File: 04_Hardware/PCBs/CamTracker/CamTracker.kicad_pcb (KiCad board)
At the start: 6 copper layers, 126.2 x 49.2 mm, 403 parts, among them IC1 W25Q128JVSIM, IC2 AP7361E-33FGE-7, IC3 AP7361E-33FGE-7, J1 PJ-059A, J10 1.25x15P, J11 22-28-4034, J12 22-28-4034, J13 SIM8066-6-1-14-01-A, J14 MEM2061-01-188-00-A, J15 636101112001, J16 636101112001, J17 636101112001, J18 636101112001, J2 67996-100HLF, J21 67996-100HLF, J22 USB3076-30-A, J27 53047-0210, J28 Bus_M.2_Socket_M, J3 67996-100HLF, J5 22-28-4034, J6 USB4080-03-A, J7 22-28-4044, J9 1.25x15P, Q1 BC817-40,215, Q10 BC817-40,215, Q11 BC817-40,215, Q2 BC817-40,215, Q3 BC817-40,215, Q4 BC817-40,215, Q5 BC817-40,215, Q6 BC817-40,215, Q9 BC817-40,215, U1 SC206EEMDA-G51-UGNDA, U10 SGM804, U11 ST4SI2M0020TPIFW, U12 RP2040, U13 PAM8302AASCR, U14 ASM2362, U15 AP61100Z6-7, U2 AP64502QSP-13, U3 AP7335-WG-7, U4 AP22654QWU-7, U6 AP61300Z6-7, U7 PI3USB4000DZUAEX, U9 PI3USB4000DZUAEX, Y1 ABM8-272-T3, Y2 25MHz

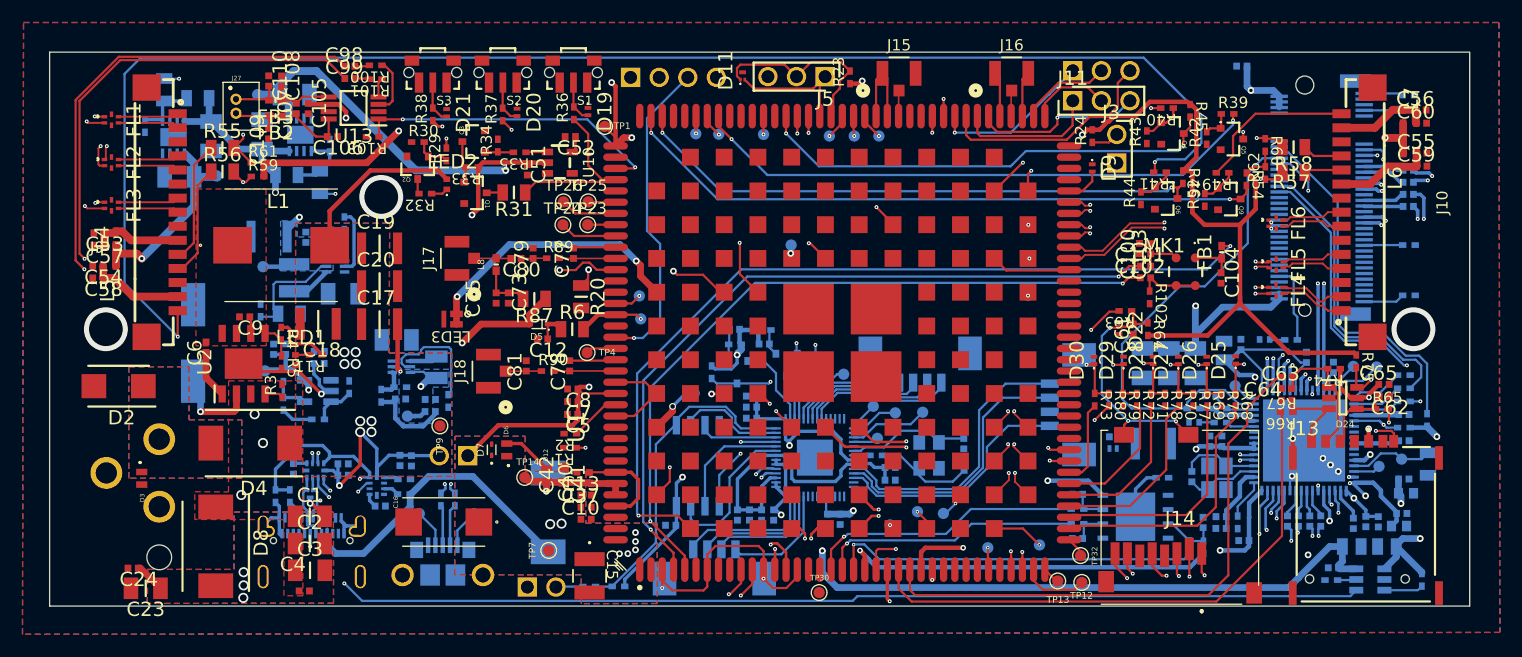
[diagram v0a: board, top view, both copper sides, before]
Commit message: feat(layout): Completed routing of all traces but with Errors DRCs
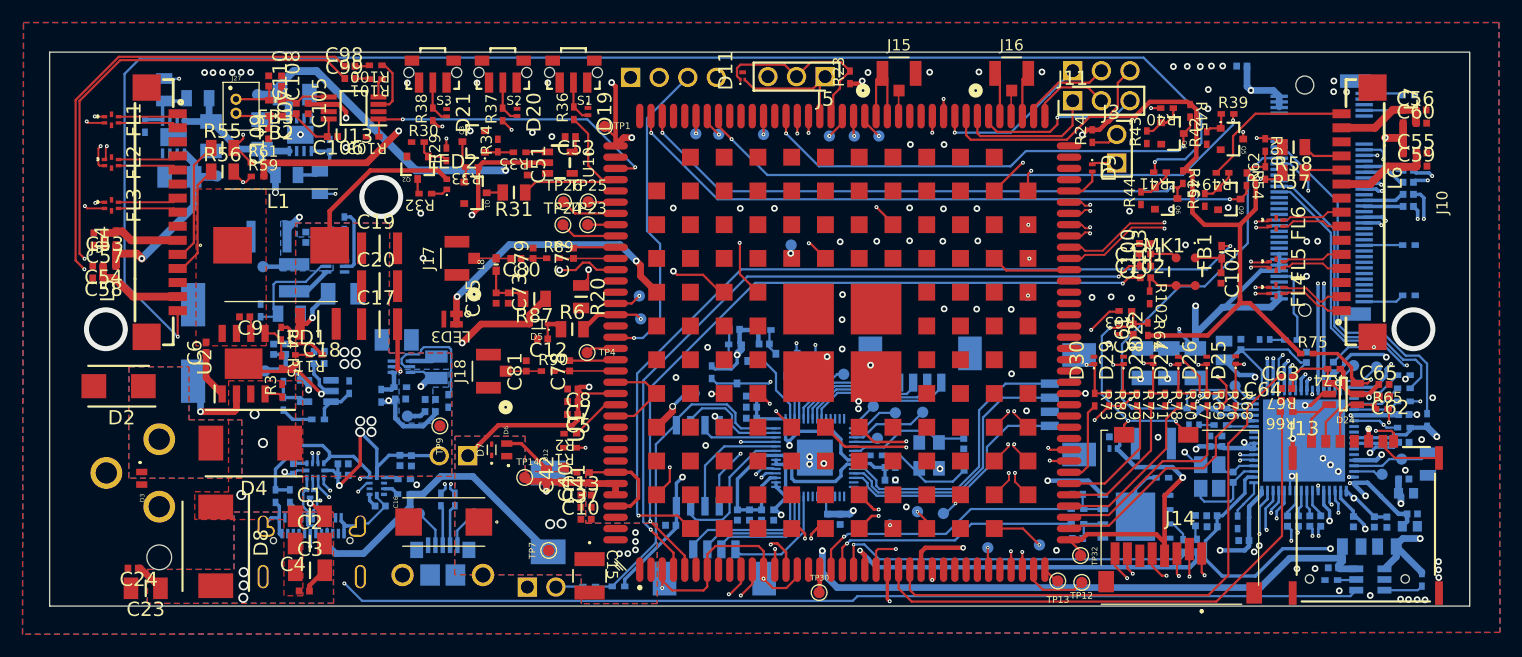
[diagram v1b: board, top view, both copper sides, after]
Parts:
- moved R75 4.43 mm to (181.5, 85.8), turned to 0 degrees
- moved C148 3.67 mm to (174.9, 96.8)
- moved C138 0.96 mm to (190.6, 101.2)
- moved C140 0.94 mm to (190.8, 100.1)
- moved C147 0.82 mm to (173.0, 100.2)
- moved C142 0.79 mm to (173.1, 101.2)
- moved C129 0.76 mm to (187.5, 100.8)
- moved C133 0.76 mm to (188.6, 100.8)
- moved TP39 0.75 mm to (188.1, 96.5)
- moved C70 0.70 mm to (171.6, 100.7)
- moved Y2 0.65 mm to (172.8, 96.7)
- moved R83 0.59 mm to (170.5, 102.9)
- moved R84 0.59 mm to (171.7, 102.9)
- moved D24 0.36 mm to (184.7, 89.4)
- moved LED5 0.22 mm to (171.4, 92.1)
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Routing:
- net NVMe_1V05: track 179.3 -> 225.9 mm, vias 7 -> 11
- net GND: track 134.3 -> 174.2 mm, vias 15 -> 121
- net NVMe_3V3: track 253.4 -> 292.1 mm, vias 6 -> 10
- net /SIM_SD/SD_VDD: track 1.82 -> 29.3 mm, vias 0 -> 1
- net SD_LDO4: track 36.4 -> 60.2 mm, vias 2 -> 6
- net NVMe_2V5: track 37.9 -> 61.1 mm, vias 5 -> 6
- net LDO15A_1V8: track 206.7 -> 201.7 mm
- net /SIM_SD/USIM1_DET: track 73.7 -> 78.6 mm
- net Net-(U14-XO): track 7.08 -> 3.65 mm
- net Net-(U1F-SD_CLK): track 23.5 -> 20.9 mm
- net Net-(U1E-USB_BOOT): track 29.8 -> 32.0 mm
- net Net-(U1F-USIM2_DET): track 0.00 -> 2.06 mm
- net Net-(U1F-SD_CMD): track 21.0 -> 18.9 mm
- net /SIM_SD/USIM1_VDD: track 69.1 -> 70.2 mm
- net /Audio/MIC1_P: track 66.3 -> 67.4 mm
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
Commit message: feat(layout): Resolved all DRC Errors
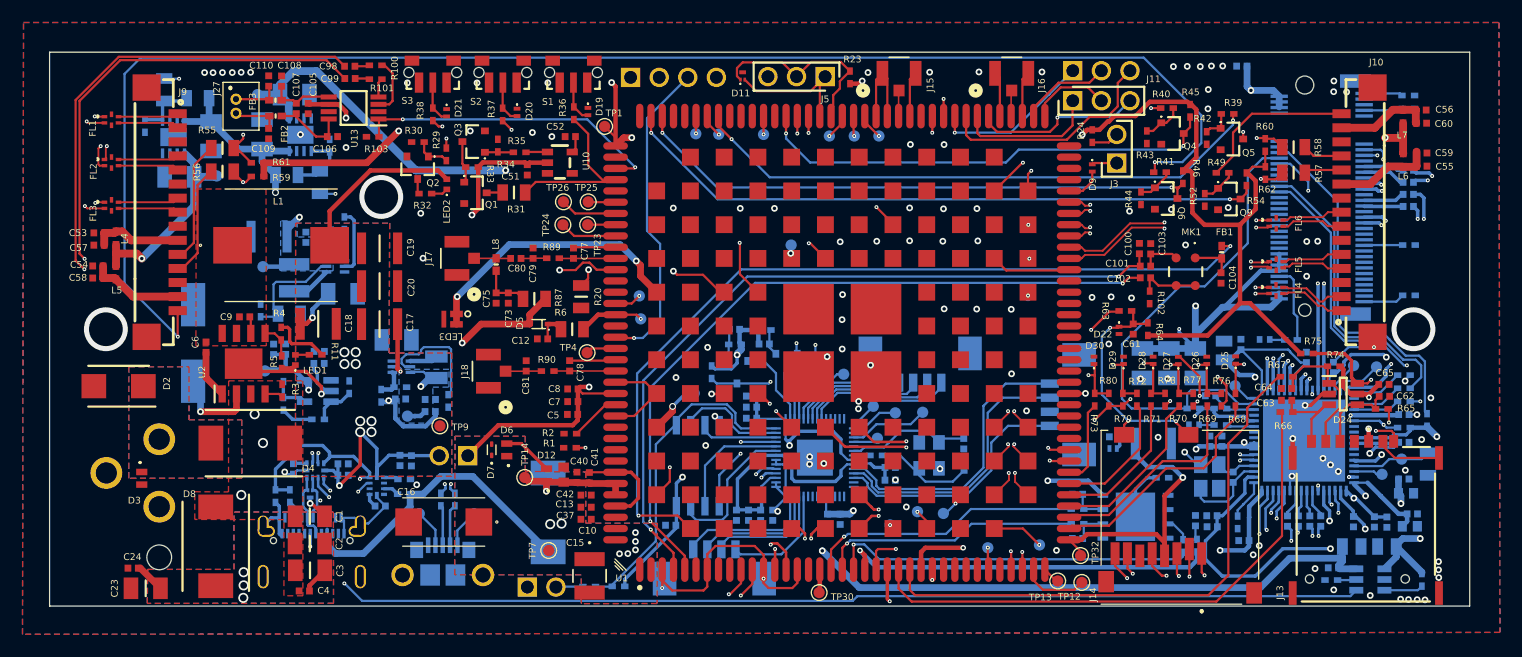
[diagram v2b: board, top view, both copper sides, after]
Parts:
- moved R98 0.79 mm to (137.5, 86.6), turned to -90 degrees
- moved R74 0.22 mm to (183.9, 86.9)
- moved C84 0.09 mm to (132.9, 100.2)
- moved C85 0.09 mm to (130.8, 100.2)
- moved C86 0.09 mm to (131.8, 100.2)
- moved C92 0.09 mm to (134.0, 100.2)
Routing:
- net VREG_3V3: track 167.8 -> 162.3 mm
- net GND: track 174.2 -> 179.1 mm
- net VUSB_BUS: track 93.1 -> 91.9 mm
- net /SIM_SD/SD_VDD: track 29.3 -> 28.5 mm
- net /MCU/MCU_UART_RX: track 5.72 -> 6.58 mm
- net /USB_UARTs/USB_SW: track 122.5 -> 123.2 mm
- net LDO15A_1V8: track 201.7 -> 201.1 mm
- net Net-(J14-CD/DAT3): track 29.6 -> 29.0 mm
- net NVMe_1V05: track 225.9 -> 226.5 mm, vias 11 -> 10
- net NVMe_2V5: track 61.1 -> 60.7 mm, vias 6 -> 5
